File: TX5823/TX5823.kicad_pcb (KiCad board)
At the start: 4 copper layers, 93 parts, among them IC1 ATMEGA328P-A, IC2 ATTINY13A-SS, P1 Akku_in, P2 ISP, P3 Mavlink, P4 CONN_01X01, P5 CONN_01X01, P6 CONN_01X01, P7 CONN_01X01, Q1 MOSFET_P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

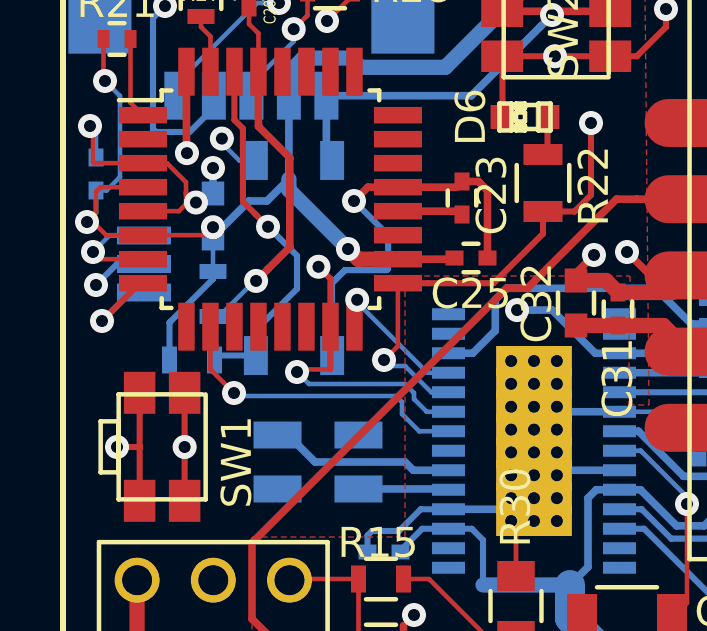
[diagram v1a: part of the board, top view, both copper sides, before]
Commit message: Lötstop richtig eingestellt
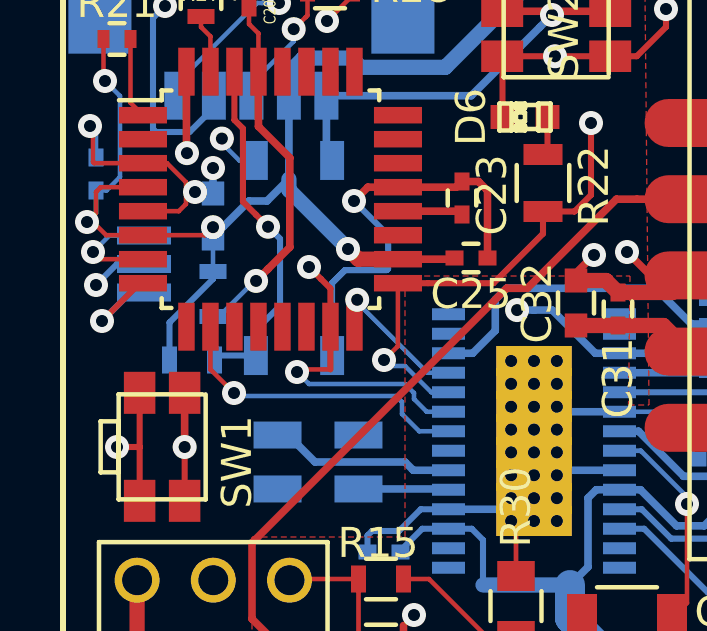
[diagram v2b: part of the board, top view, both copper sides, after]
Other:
- rule pad_to_mask_clearance: 0 -> 0.15
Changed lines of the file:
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@@
     (thickness 1.6)
     (drawings 4)
-    (tracks 1130)
+    (tracks 1127)
     (zones 0)
     (modules 93)
@@
   )
   (setup
-    (last_trace_width 0.4)
+    (last_trace_width 0.254)
     (user_trace_width 0.1524)
     (user_trace_width 0.16)
@@
     (pad_size 1.9 1.9)
     (pad_drill 1.016)
-    (pad_to_mask_clearance 0)
+    (pad_to_mask_clearance 0.15)
+    (solder_mask_min_width 0.15)
     (aux_axis_origin 0 0)
     (visible_elements FFFEFF7F)
     (pcbplotparams
-      (layerselection 0x00000_80000000)
+      (layerselection 0x00000_00000001)
       (usegerberextensions false)
       (excludeedgelayer true)
@@
       (subtractmaskfromsilk false)
       (outputformat 2)
-      (mirror true)
+      (mirror false)
       (drillshape 0)
       (scaleselection 1)
@@
   (segment (start 80 68.6) (end 85.6 68.6) (width 1) (layer B.Cu) (net 1))
   (segment (start 77.6 64.24) (end 77.6 66.2) (width 1) (layer B.Cu) (net 1))
+  (segment (start 79.1 27.7) (end 79.4 27.7) (width 0.1524) (layer F.Cu) (net 2))
+  (via (at 79.4 27.7) (size 0.8) (drill 0.4) (layers F.Cu B.Cu) (net 2))
   (segment (start 93.05 64.1) (end 93.05 65) (width 0.254) (layer B.Cu) (net 2))
   (segment (start 93.05 65) (end 93.55 65.5) (width 0.254) (layer B.Cu) (net 2))
@@
   (segment (start 80 27.75) (end 80 26.9) (width 0.254) (layer B.Cu) (net 2))
   (via (at 80 26.9) (size 0.8) (drill 0.4) (layers F.Cu B.Cu) (net 2))
-  (segment (start 79.381281 28.050308) (end 79.431462 28.050308) (width 0.1524) (layer F.Cu) (net 2))
-  (segment (start 79.1 27.7) (end 79.1 27.769027) (width 0.1524) (layer F.Cu) (net 2))
-  (via (at 79.431462 28.050308) (size 0.8) (drill 0.4) (layers F.Cu B.Cu) (net 2))
-  (segment (start 79.1 27.769027) (end 79.381281 28.050308) (width 0.1524) (layer F.Cu) (net 2))
   (segment (start 96.15 35.4) (end 95.95 35.2) (width 0.1524) (layer B.Cu) (net 2))
   (segment (start 93.55 35.025) (end 95.775 35.025) (width 0.1524) (layer B.Cu) (net 2) (status 10))
@@
   (segment (start 82.561797 29.538203) (end 81.835918 30.264082) (width 0.254) (layer F.Cu) (net 6))
   (segment (start 81.515 23.69) (end 81.515 25.515) (width 0.254) (layer F.Cu) (net 6))
-  (segment (start 79.055 33.045) (end 81.03592 31.06408) (width 0.2032) (layer Signal) (net 6))
-  (segment (start 79.055 36.2) (end 79.055 33.045) (width 0.2032) (layer Signal) (net 6))
+  (segment (start 79.055 33.045) (end 81.03592 31.06408) (width 0.254) (layer Signal) (net 6))
+  (segment (start 79.055 36.2) (end 79.055 33.045) (width 0.254) (layer Signal) (net 6))
   (segment (start 81.385919 30.664081) (end 81.435919 30.664081) (width 0.1524) (layer B.Cu) (net 6))
   (segment (start 81.515 25.515) (end 82.561797 26.561797) (width 0.254) (layer F.Cu) (net 6))
@@
   (segment (start 81.215 21.565) (end 81.2 21.55) (width 0.1524) (layer F.Cu) (net 6) (status 30))
   (segment (start 79.055 36.2) (end 79.055 37.995) (width 0.2032) (layer F.Cu) (net 6))
-  (segment (start 79.055 34.395) (end 79.055 36.2) (width 0.2032) (layer F.Cu) (net 6))
+  (segment (start 79.055 34.395) (end 79.055 36.2) (width 0.254) (layer F.Cu) (net 6))
   (via (at 79.055 36.2) (size 0.8) (drill 0.4) (layers F.Cu B.Cu) (net 6))
   (segment (start 81.2 20.45) (end 81.85 20.45) (width 0.1524) (layer F.Cu) (net 7))
@@
   (segment (start 77.25 22.6) (end 77.25 24.725) (width 0.1524) (layer F.Cu) (net 20))
   (segment (start 77.25 24.725) (end 77.665 25.14) (width 0.1524) (layer F.Cu) (net 20))
-  (segment (start 82.234795 29.258444) (end 81.834796 28.858445) (width 0.2032) (layer B.Cu) (net 21))
-  (segment (start 82.8 29.823649) (end 82.234795 29.258444) (width 0.2032) (layer B.Cu) (net 21))
-  (segment (start 82.8 30.92776) (end 82.8 29.823649) (width 0.2032) (layer B.Cu) (net 21))
-  (segment (start 81.43 32.29776) (end 82.8 30.92776) (width 0.2032) (layer B.Cu) (net 21))
+  (segment (start 82.234795 31.492965) (end 82.234795 29.258444) (width 0.2032) (layer B.Cu) (net 21))
+  (segment (start 81.43 32.29776) (end 82.234795 31.492965) (width 0.2032) (layer B.Cu) (net 21))
   (segment (start 81.43 33.1512) (end 81.43 32.29776) (width 0.2032) (layer B.Cu) (net 21))
+  (segment (start 82.234795 29.258444) (end 81.834796 28.858445) (width 0.2032) (layer B.Cu) (net 21))
   (segment (start 80.715 23.69) (end 80.715 25.300271) (width 0.2032) (layer F.Cu) (net 21))
   (segment (start 80.715 25.300271) (end 80.997279 25.58255) (width 0.2032) (layer F.Cu) (net 21))
@@
   (segment (start 77.56 30.74) (end 76.3 32) (width 0.2032) (layer F.Cu) (net 23))
   (segment (start 77.665 30.74) (end 77.56 30.74) (width 0.2032) (layer F.Cu) (net 23))
-  (segment (start 83.515358 29.626717) (end 83.515358 30.192402) (width 0.2032) (layer Signal) (net 24))
-  (segment (start 83.515358 29.546272) (end 83.515358 29.626717) (width 0.2032) (layer Signal) (net 24))
-  (segment (start 101.9 29.3) (end 101.498399 28.898399) (width 0.2032) (layer Signal) (net 24))
-  (segment (start 84.163231 28.898399) (end 83.515358 29.546272) (width 0.2032) (layer Signal) (net 24))
-  (segment (start 101.498399 28.898399) (end 84.163231 28.898399) (width 0.2032) (layer Signal) (net 24))
-  (segment (start 83.915 32.19) (end 83.915 30.592044) (width 0.2032) (layer F.Cu) (net 24))
-  (segment (start 83.915 30.592044) (end 83.515358 30.192402) (width 0.2032) (layer F.Cu) (net 24))
-  (via (at 83.515358 30.192402) (size 0.8) (drill 0.4) (layers F.Cu B.Cu) (net 24))
+  (segment (start 83.915 30.915) (end 83.599999 30.599999) (width 0.2032) (layer F.Cu) (net 24))
+  (segment (start 83.2 29.634315) (end 83.2 30.2) (width 0.2032) (layer Signal) (net 24))
+  (segment (start 83.915 32.19) (end 83.915 30.915) (width 0.2032) (layer F.Cu) (net 24))
+  (segment (start 101.9 29.3) (end 101.500001 28.900001) (width 0.2032) (layer Signal) (net 24))
+  (via (at 83.2 30.2) (size 0.8) (drill 0.4) (layers F.Cu B.Cu) (net 24))
+  (segment (start 101.500001 28.900001) (end 83.934314 28.900001) (width 0.2032) (layer Signal) (net 24))
+  (segment (start 83.934314 28.900001) (end 83.2 29.634315) (width 0.2032) (layer Signal) (net 24))
+  (segment (start 83.599999 30.599999) (end 83.2 30.2) (width 0.2032) (layer F.Cu) (net 24))
   (via (at 101.9 29.3) (size 0.8) (drill 0.4) (layers F.Cu B.Cu) (net 24))
   (segment (start 101.9 22.16) (end 101.9 29.3) (width 0.2032) (layer B.Cu) (net 24))
@@
   (segment (start 100.7 25.3) (end 100.63 25.37) (width 0.2032) (layer B.Cu) (net 26))
   (via (at 100.7 25.3) (size 0.8) (drill 0.4) (layers F.Cu B.Cu) (net 26))
-  (segment (start 92.7 25.3) (end 100.7 25.3) (width 0.2032) (layer Signal) (net 26))
+  (segment (start 92.7 25.3) (end 100.7 25.3) (width 0.254) (layer Signal) (net 26))
   (segment (start 92.6 25.4) (end 92.7 25.3) (width 0.2032) (layer Signal) (net 26))
   (via (at 92.6 25.4) (size 0.8) (drill 0.4) (layers F.Cu B.Cu) (net 26))
@@
   (segment (start 83.400001 22.399999) (end 83.400001 22.814996) (width 0.1524) (layer Signal) (net 37))
   (segment (start 83.8 22) (end 83.400001 22.399999) (width 0.1524) (layer Signal) (net 37))
-  (segment (start 83.400001 22.814996) (end 80.295678 25.919319) (width 0.1524) (layer Signal) (net 37))
+  (segment (start 83.400001 22.814996) (end 80.295678 25.919319) (width 0.254) (layer Signal) (net 37))
   (segment (start 80.295678 26.066928) (end 80.295678 25.919319) (width 0.1524) (layer B.Cu) (net 37))
   (via (at 80.295678 25.919319) (size 0.8) (drill 0.4) (layers F.Cu B.Cu) (net 37))
@@
   (segment (start 120.5 63) (end 120.6 63) (width 0.1524) (layer B.Cu) (net 109))
   (segment (start 120.6 63) (end 121.3 63) (width 0.4) (layer B.Cu) (net 109))
-  (segment (start 121.9 62.7) (end 121.3 62.7) (width 0.1524) (layer B.Cu) (net 109) (status 400000))
-  (segment (start 121.3 63.2) (end 121.9 63.2) (width 0.1524) (layer B.Cu) (net 109) (status 800000))
+  (segment (start 121.9 62.7) (end 121.3 62.7) (width 0.1524) (layer B.Cu) (net 109))
+  (segment (start 121.3 63.2) (end 121.9 63.2) (width 0.1524) (layer B.Cu) (net 109))
   (segment (start 121.3 62.7) (end 121.3 63) (width 0.1524) (layer B.Cu) (net 109))
   (segment (start 121.3 63) (end 121.3 63.2) (width 0.1524) (layer B.Cu) (net 109))
   (segment (start 123 62.9) (end 124 62.9) (width 0.4) (layer B.Cu) (net 110))
-  (segment (start 122.4 62.7) (end 123 62.7) (width 0.1524) (layer B.Cu) (net 110) (status 400000))
-  (segment (start 123 63.2) (end 122.4 63.2) (width 0.1524) (layer B.Cu) (net 110) (status 800000))
+  (segment (start 122.4 62.7) (end 123 62.7) (width 0.1524) (layer B.Cu) (net 110))
+  (segment (start 123 63.2) (end 122.4 63.2) (width 0.1524) (layer B.Cu) (net 110))
   (segment (start 123 62.7) (end 123 62.9) (width 0.1524) (layer B.Cu) (net 110))
   (segment (start 123 62.9) (end 123 63.2) (width 0.1524) (layer B.Cu) (net 110))
-  (segment (start 122.4 63.7) (end 124 63.7) (width 0.1524) (layer B.Cu) (net 111) (status 400000))
-  (segment (start 121.9 63.7) (end 120.5 63.7) (width 0.1524) (layer B.Cu) (net 112) (status 400000))
+  (segment (start 122.4 63.7) (end 124 63.7) (width 0.1524) (layer B.Cu) (net 111))
+  (segment (start 121.9 63.7) (end 120.5 63.7) (width 0.1524) (layer B.Cu) (net 112))
   (zone (net 97) (net_name /5,2V) (layer F.Cu) (hatch edge 0.508)
     (connect_pads yes (clearance 0.6))

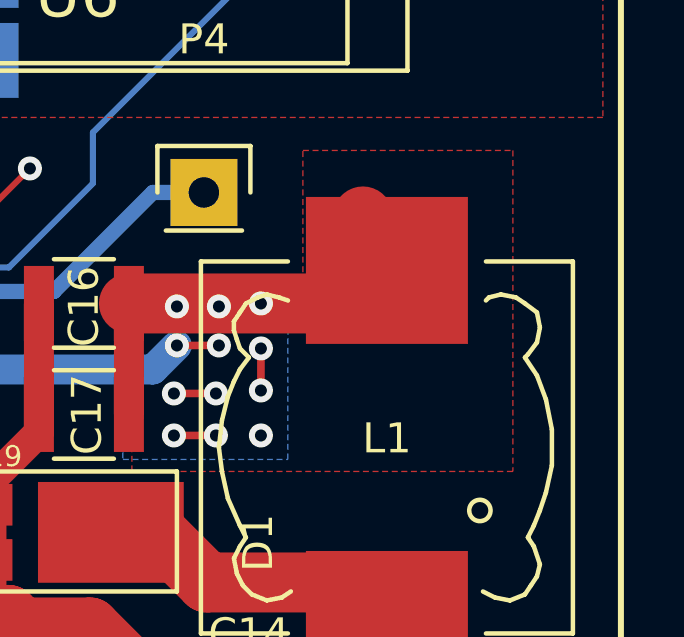
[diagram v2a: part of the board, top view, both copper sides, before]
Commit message: logo hinzugefügt
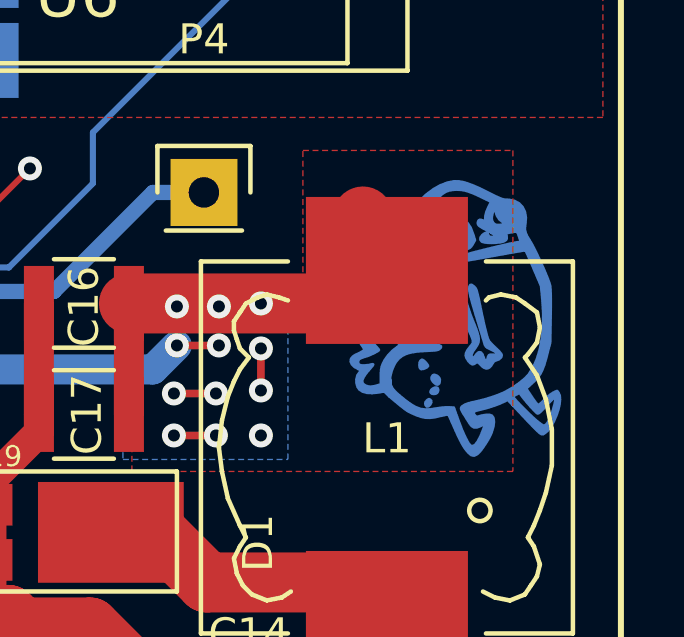
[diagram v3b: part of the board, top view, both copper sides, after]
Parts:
- added G***: LOGO, toni:Kupferdickbutt, B.Cu at (119.3, 48.2)

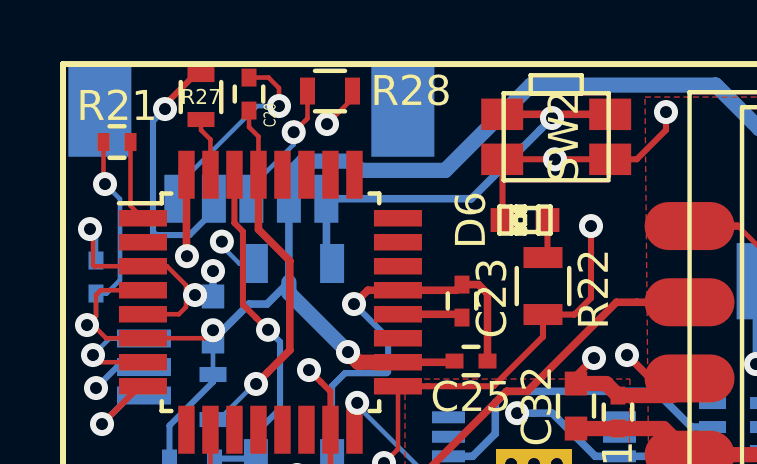
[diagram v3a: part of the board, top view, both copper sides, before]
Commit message: Vias vom Rand weggerückt github link hinzugefügt
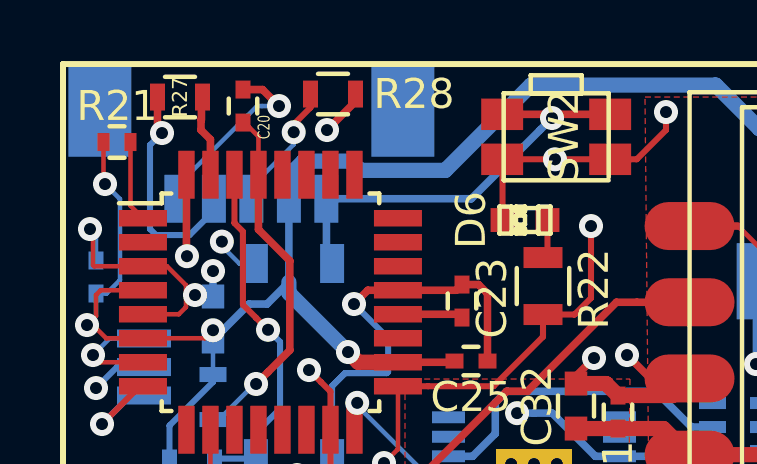
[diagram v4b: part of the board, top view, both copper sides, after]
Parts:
- moved R27 0.70 mm to (78.9, 21.1), turned to 0 degrees
- moved C20 0.45 mm to (81.0, 21.4)
- moved R28 0.14 mm to (84.0, 21.0)
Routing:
- net Net-(P3-Pad2): track 9.52 -> 8.26 mm
- net /TXO: track 1.99 -> 2.77 mm
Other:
- board text added: "https://github.com/ep092 v0.1"

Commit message: letzte Änderungen für Fertigung Gerberdaten hinzugefügt
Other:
- board outline added: 50 x 50 mm

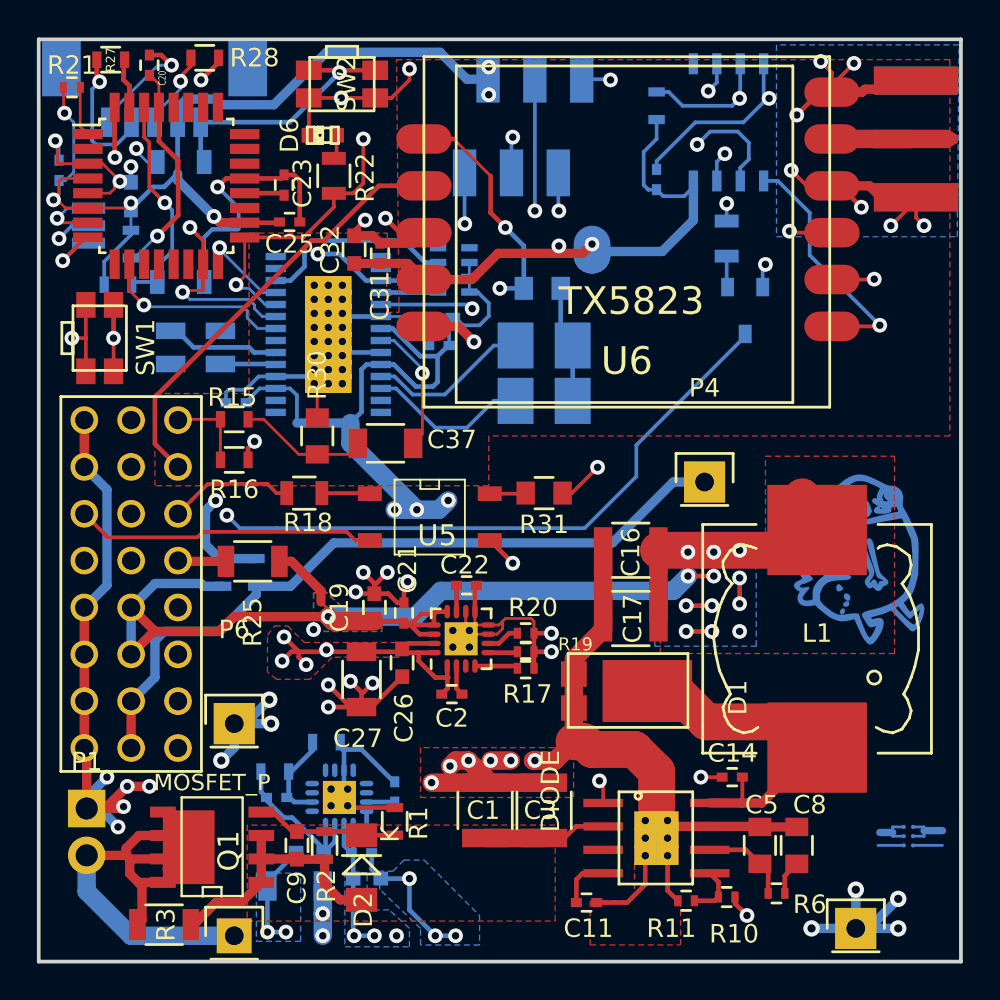
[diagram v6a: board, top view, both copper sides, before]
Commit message: mavlink und adum geroutet
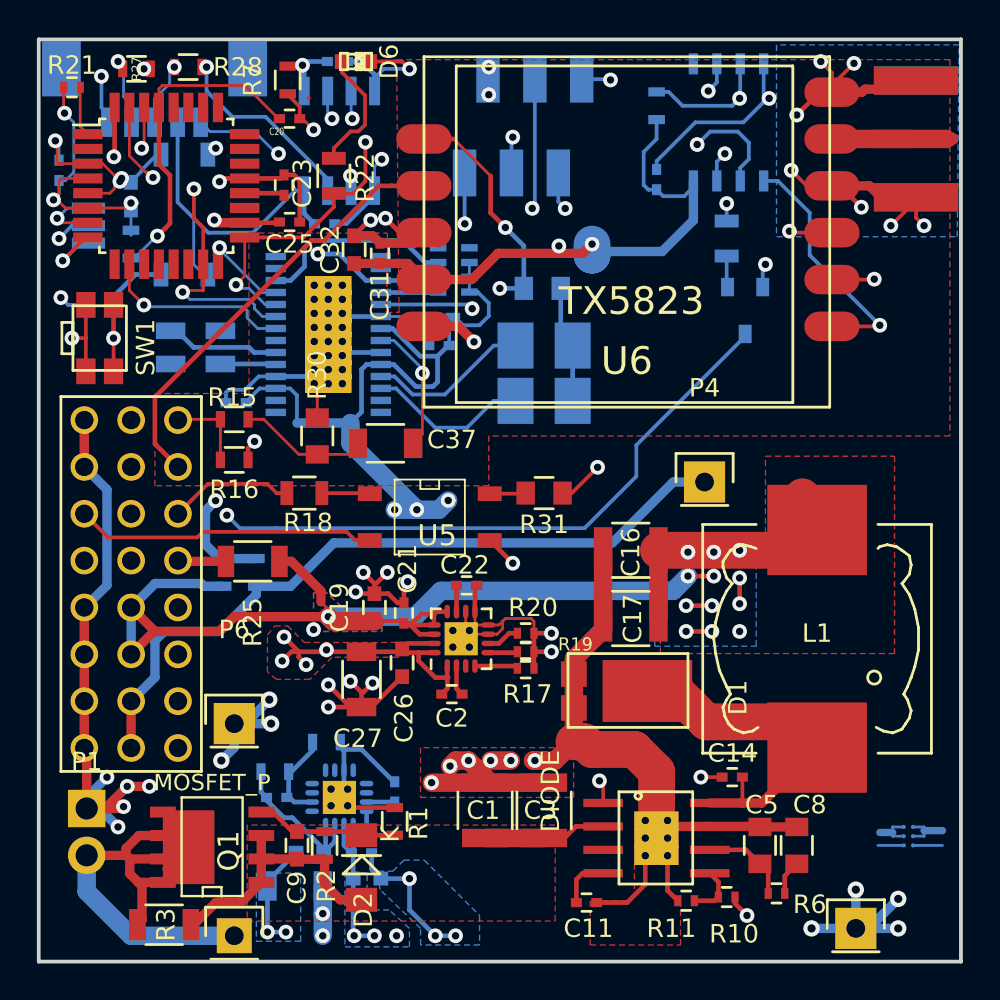
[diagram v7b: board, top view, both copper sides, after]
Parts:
- removed G***: LOGO, toni:Kupferdickbutt
- removed R26: open, Resistors_SMD:R_0603
- removed SW2: SW_PUSH, toni:EVQP7A
- added C15: 100nF, Capacitors_SMD:C_0402, B.Cu at (91.2, 21.2)
- added C18: 100nF, Capacitors_SMD:C_0402, B.Cu at (90.5, 30.0)
- added R7: 10k, Resistors_SMD:R_0603, F.Cu at (88.5, 22.2)
- added R8: 300R, Resistors_SMD:R_0603, B.Cu at (78.4, 34.4)
- added U10: OPTO-TRANSISTOR4, toni:SO-4, B.Cu at (82.9, 29.5)
- R27: value 100R -> 1k
- R28: value 300R -> 1k
- U8: value OPTO-TRANSISTOR4 -> ADuM1201AR; footprint toni:SO-4 -> Housings_SOIC:SOIC-8_3.9x4.9mm_Pitch1.27mm
- moved U8 9.66 mm to (91.3, 25.5), turned to 270 degrees
- moved C20 8.13 mm to (88.6, 24.3), turned to 0 degrees
- moved D6 4.39 mm to (92.2, 21.2), turned to 0 degrees
- moved R27 1.49 mm to (80.3, 21.6)
- moved R28 1.03 mm to (83.1, 21.5)
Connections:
- P3 pad 1: /DTR -> Net-(P3-Pad1)
- P3 pad 4: +5V -> Net-(C18-Pad1)
- P3 pad 5: Net-(P3-Pad5) -> Net-(C18-Pad2)
- R27 pad 2: /TXO -> Net-(R27-Pad2)
- U8 pad 1: Net-(R28-Pad2) -> +5V
- U8 pad 2: Net-(P3-Pad5) -> /RXI
- U8 pad 3: GND -> /TXO
- U8 pad 4: /RXI -> GND
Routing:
- net Net-(R27-Pad2): track 0.00 -> 20.3 mm, vias 0 -> 2
- net Net-(C18-Pad1): track 0.00 -> 18.4 mm
- net Net-(P3-Pad1): track 0.00 -> 17.6 mm, vias 0 -> 2
- net Net-(C18-Pad2): track 0.00 -> 15.7 mm, vias 0 -> 2
- net /TXO: track 2.77 -> 18.3 mm, vias 0 -> 2
- net Net-(P3-Pad5): track 14.9 -> 0.00 mm, vias 1 -> 0
- net GND: track 301.2 -> 288.0 mm, vias 55 -> 54
- net +5V: track 176.6 -> 189.6 mm, vias 11 -> 12
- net /RESET: track 57.2 -> 64.1 mm
- net Net-(D6-Pad1): track 1.31 -> 6.93 mm
- net /RXI: track 11.9 -> 15.9 mm, vias 1 -> 2
- net Net-(R8-Pad2): track 0.00 -> 3.49 mm
- net Net-(P3-Pad2): track 8.26 -> 5.18 mm
- net /DTR: track 6.36 -> 8.91 mm, vias 1 -> 2
- net Net-(R28-Pad2): track 8.37 -> 10.8 mm, vias 2 -> 1
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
